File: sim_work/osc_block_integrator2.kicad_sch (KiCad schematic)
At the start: 6 parts, among them U1 ADA4530-1

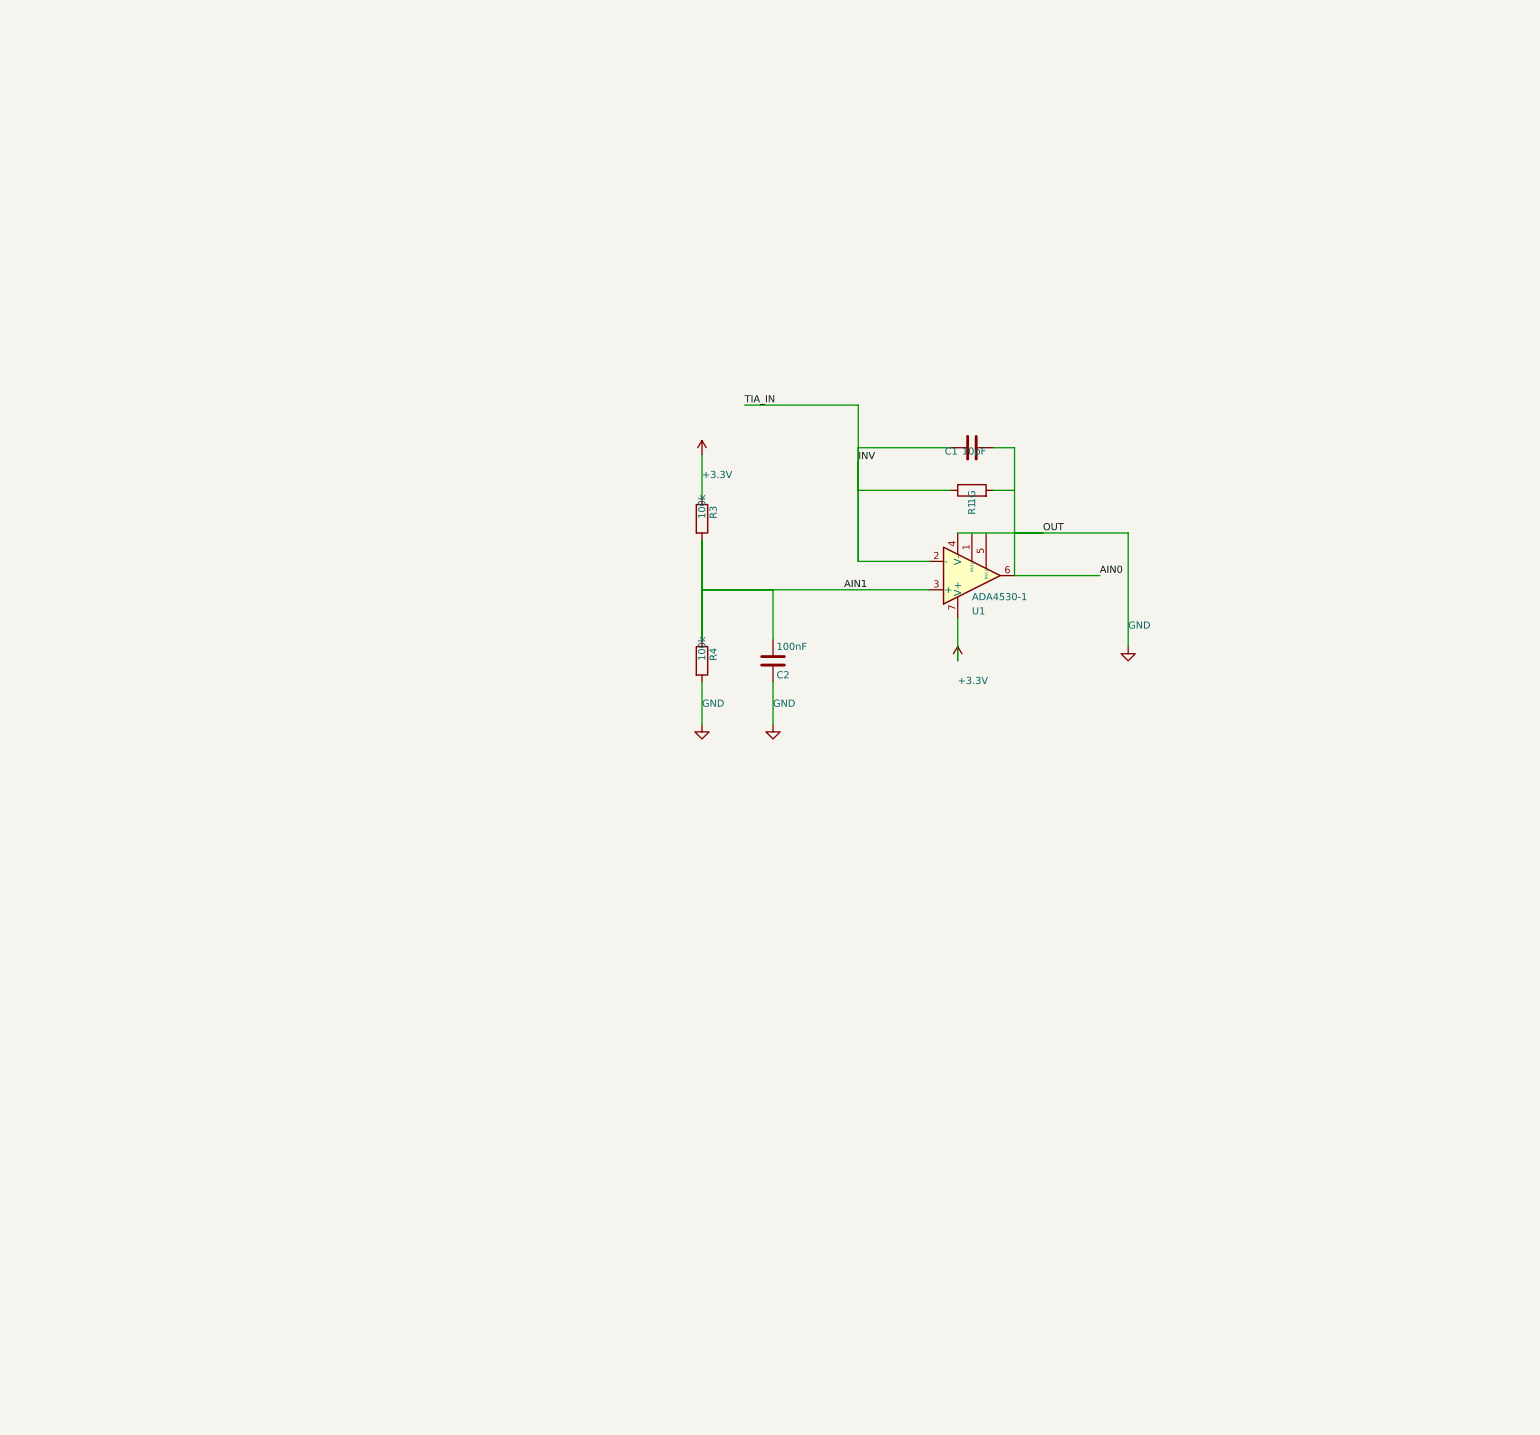
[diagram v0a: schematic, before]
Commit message: Per-block PDF schematics: 6 oscillator + 6 TIA blocks with merged PDFs
Add individual A4 schematic generation for each functional circuit block:
- Oscillator: summing amp, integrator 1/2, RMS detector, power supply, MCU
- TIA: input filters, analog mux, mux TIA, relay ladder, MCU section, electrometer
- merge_pdfs() helper using PyMuPDF for multi-page output
- CLI commands: osc_blocks, tia_blocks
- All blocks verified: 0 wire crossings, complete pin connectivity

Co-Authored-By: Claude Opus 4.6 <noreply@anthropic.com>
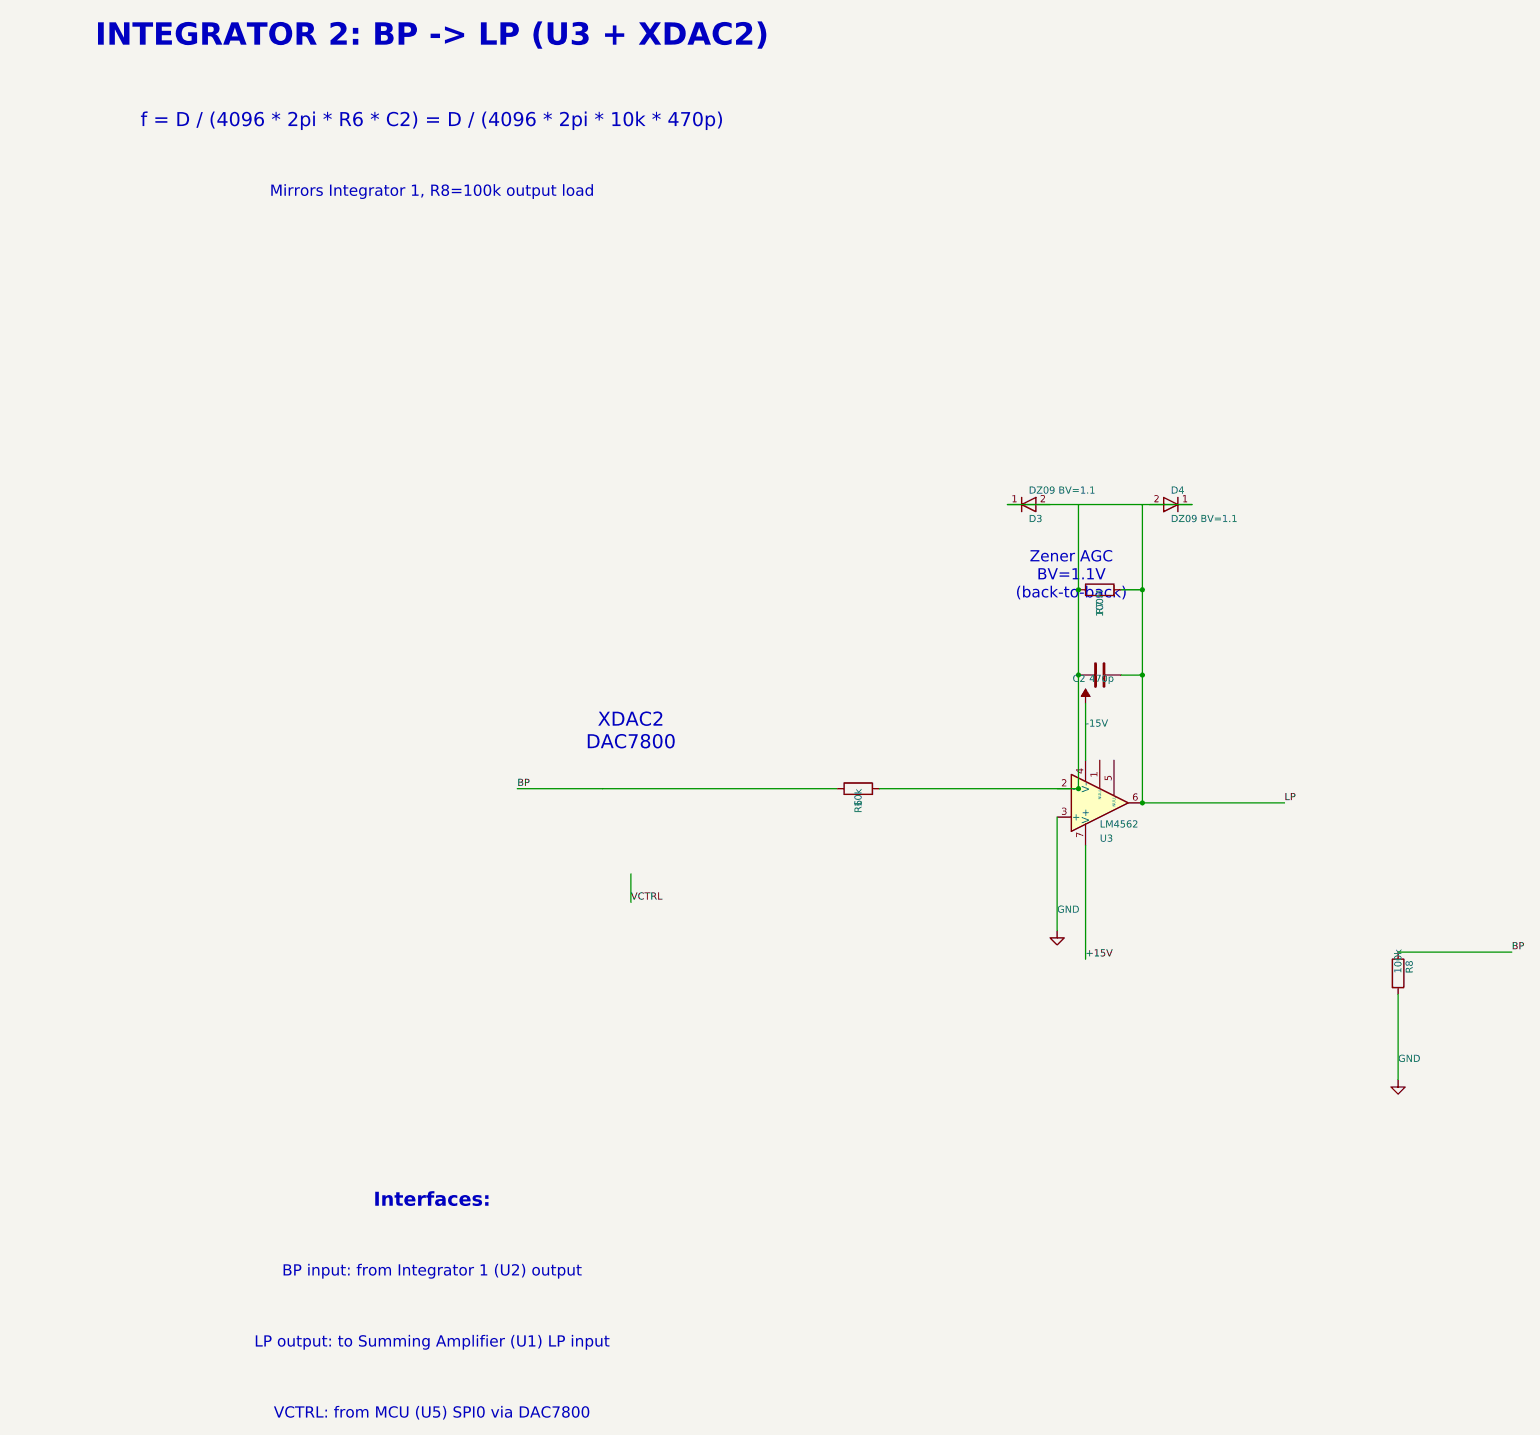
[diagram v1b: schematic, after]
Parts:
- removed C1: 10pF, symbol C:C
- removed R1: 1G, symbol R:R
- removed R3, R4: 100k, symbol R:R
- removed U1: ADA4530-1, symbol LM741:LM741
- added D3, D4: DZ09 BV=1.1, symbol D:D
- added R6: 10k, symbol R:R
- added R7: 100M, symbol R:R
- added R8: 100k, symbol R:R
- added U3: LM4562, symbol LM741:LM741
- C2: value 100nF -> 470p
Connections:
- net GND: now also R8.2, U3.3 (+); no longer C2.2
- net AIN1: no longer names the net of C2.1
- net AIN1: now also R6.2, R7.1
- new net: D3.1 (K), D4.1 (K)
- new net +15V: U3.7 (V+)
- new net -15V: U3.4 (V-)
- new net BP: R6.1, R8.1
- new net LP: C2.2, R7.2, U3.6
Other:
- note added: "BP input: from Integrator 1 (U2) output"
- note added: "INTEGRATOR 2: BP -> LP (U3 + XDAC2)"
- note added: "Interfaces:"
- note added: "LP output: to Summing Amplifier (U1) LP input"
- note added: "Mirrors Integrator 1, R8=100k output load"
- note added: "VCTRL: from MCU (U5) SPI0 via DAC7800"
- note added: "XDAC2 DAC7800"
- note added: "Zener AGC BV=1.1V (back-to-back)"
- note added: "f = D / (4096 * 2pi * R6 * C2) = D / (4096 * 2pi * 10k * 470p)"
- company: (none) -> CircuitForge
- title: TIA with Mux Interface - ADA4530-1 -> State Variable Oscillator - Integrator 2 (BP to LP)
